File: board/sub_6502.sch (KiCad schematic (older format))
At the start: 17 parts, among them Q1201 Q_NPN_BEC, U1201 74HCT245, U1202 6502, U1203 74HCT245, U1204 74HCT245, U1205 74HCT245

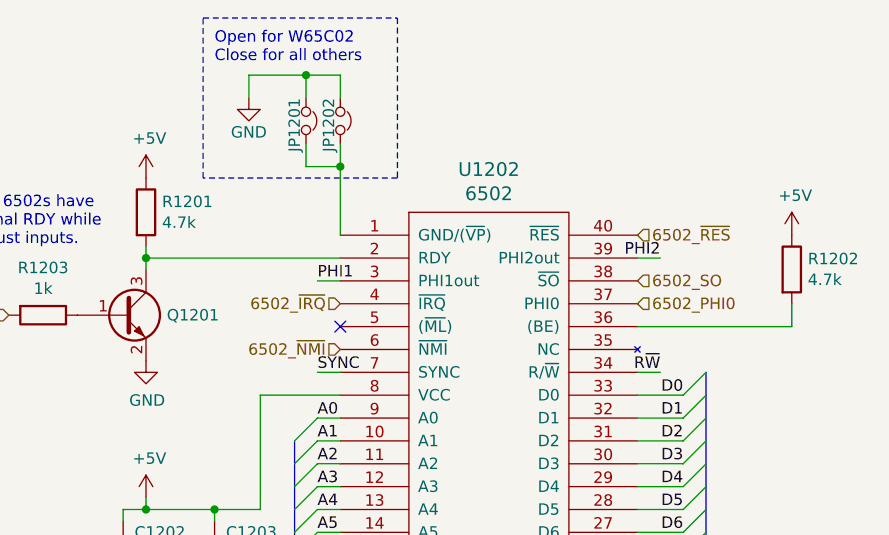
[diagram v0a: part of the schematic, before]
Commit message: Started picking footprints. Merged many components.
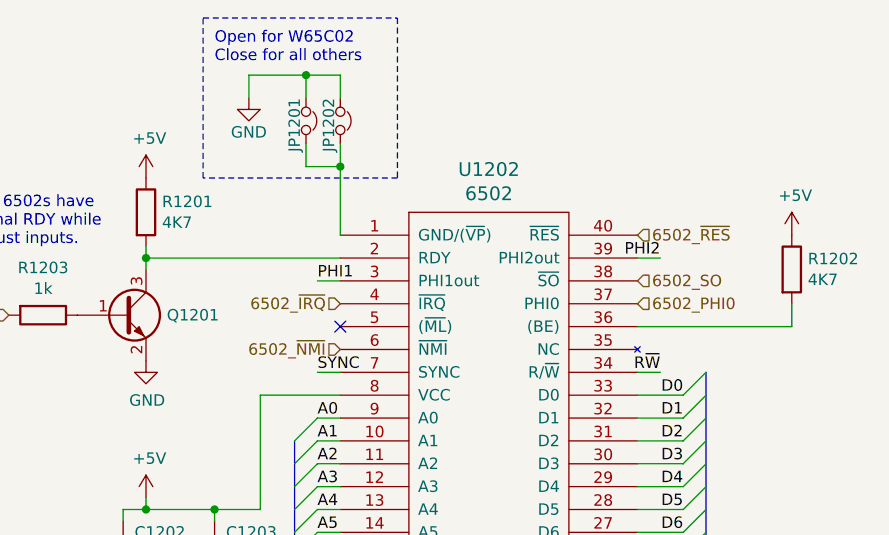
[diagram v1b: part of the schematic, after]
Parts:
- R1201, R1202: value 4.7k -> 4K7
- U1201, U1203, U1204, U1205: footprint (none) -> Package_SO:SSOP-20_4.4x6.5mm_P0.65mm
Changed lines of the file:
@@
 $Descr A4 11693 8268
 encoding utf-8
-Sheet 12 14
+Sheet 12 15
 Title ""
 Date ""
@@
 F 0 "U1202" H 9200 3687 60  0000 C CNN
 F 1 "6502" H 9200 3581 60  0000 C CNN
-F 2 "" H 8700 2700 60  0000 C CNN
+F 2 "" H 8700 2700 60  0001 C CNN
 F 3 "" H 8700 2700 60  0000 C CNN
 	1    9200 2500
@@
 F 0 "U1205" H 9150 5650 50  0000 C CNN
 F 1 "74HCT245" H 9600 5650 50  0000 C CNN
-F 2 "" H 9350 5000 50  0001 C CNN
+F 2 "Package_SO:SSOP-20_4.4x6.5mm_P0.65mm" H 9350 5000 50  0001 C CNN
 F 3 "http://www.ti.com/lit/gpn/sn74HC245" H 9350 5000 50  0001 C CNN
 	1    9350 5000
@@
 F 0 "U1203" H 4900 5650 50  0000 C CNN
 F 1 "74HCT245" H 5350 5650 50  0000 C CNN
-F 2 "" H 5100 5000 50  0001 C CNN
+F 2 "Package_SO:SSOP-20_4.4x6.5mm_P0.65mm" H 5100 5000 50  0001 C CNN
 F 3 "http://www.ti.com/lit/gpn/sn74HC245" H 5100 5000 50  0001 C CNN
 	1    5100 5000
@@
 F 0 "U1204" H 6700 5650 50  0000 C CNN
 F 1 "74HCT245" H 7150 5650 50  0000 C CNN
-F 2 "" H 6900 5000 50  0001 C CNN
+F 2 "Package_SO:SSOP-20_4.4x6.5mm_P0.65mm" H 6900 5000 50  0001 C CNN
 F 3 "http://www.ti.com/lit/gpn/sn74HC245" H 6900 5000 50  0001 C CNN
 	1    6900 5000
@@
 F 0 "U1201" H 5100 3000 50  0000 C CNN
 F 1 "74HCT245" H 5550 3000 50  0000 C CNN
-F 2 "" H 5300 2350 50  0001 C CNN
+F 2 "Package_SO:SSOP-20_4.4x6.5mm_P0.65mm" H 5300 2350 50  0001 C CNN
 F 3 "http://www.ti.com/lit/gpn/sn74HC245" H 5300 2350 50  0001 C CNN
 	1    5300 2350
@@
 P 7700 1500
 F 0 "R1201" H 7770 1546 50  0000 L CNN
-F 1 "4.7k" H 7770 1455 50  0000 L CNN
+F 1 "4K7" H 7770 1455 50  0000 L CNN
 F 2 "" V 7630 1500 50  0001 C CNN
 F 3 "~" H 7700 1500 50  0001 C CNN
@@
 P 10525 1750
 F 0 "R1202" H 10595 1796 50  0000 L CNN
-F 1 "4.7k" H 10595 1705 50  0000 L CNN
+F 1 "4K7" H 10595 1705 50  0000 L CNN
 F 2 "" V 10455 1750 50  0001 C CNN
 F 3 "~" H 10525 1750 50  0001 C CNN

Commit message: More footprints done. Went with simpler test-pads.
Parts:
- JP1201, JP1202: footprint (none) -> Connector_PinHeader_2.54mm:PinHeader_1x02_P2.54mm_Vertical
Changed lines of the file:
@@
 $Descr A4 11693 8268
 encoding utf-8
-Sheet 12 15
+Sheet 12 14
 Title ""
 Date ""
@@
 F 0 "JP1201" H 8300 1050 50  0000 L CNN
 F 1 "Jumper_NC_Small" H 8400 1221 50  0001 C CNN
-F 2 "" H 8400 1100 50  0001 C CNN
+F 2 "Connector_PinHeader_2.54mm:PinHeader_1x02_P2.54mm_Vertical" H 8400 1100 50  0001 C CNN
 F 3 "~" H 8400 1100 50  0001 C CNN
 	1    8400 1100
@@
 F 0 "JP1202" H 8450 1050 50  0000 L CNN
 F 1 "WireJumper" H 8550 1200 50  0001 C CNN
-F 2 "" H 8550 1100 50  0001 C CNN
+F 2 "Connector_PinHeader_2.54mm:PinHeader_1x02_P2.54mm_Vertical" H 8550 1100 50  0001 C CNN
 F 3 "~" H 8550 1100 50  0001 C CNN
 	1    8550 1100

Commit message: Most footprints associated
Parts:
- C1201, C1202, C1204, C1205, C1206: footprint (none) -> Capacitor_SMD:C_0603_1608Metric
- C1203: footprint (none) -> Capacitor_SMD:C_1206_3216Metric
- Q1201: footprint (none) -> Package_TO_SOT_SMD:SOT-23
- R1201, R1202, R1203: footprint (none) -> Resistor_SMD:R_0603_1608Metric
- U1202: footprint (none) -> Package_DIP:DIP-40_W15.24mm
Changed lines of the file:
@@
 F 0 "U1202" H 9200 3687 60  0000 C CNN
 F 1 "6502" H 9200 3581 60  0000 C CNN
-F 2 "" H 8700 2700 60  0001 C CNN
+F 2 "Package_DIP:DIP-40_W15.24mm" H 8700 2700 60  0001 C CNN
 F 3 "" H 8700 2700 60  0000 C CNN
 	1    9200 2500
@@
 F 0 "R1203" V 7043 1950 50  0000 C CNN
 F 1 "1k" V 7134 1950 50  0000 C CNN
-F 2 "" V 7180 1950 50  0001 C CNN
+F 2 "Resistor_SMD:R_0603_1608Metric" V 7180 1950 50  0001 C CNN
 F 3 "~" H 7250 1950 50  0001 C CNN
 	1    7250 1950
@@
 F 0 "Q1201" H 7791 1950 50  0000 L CNN
 F 1 "Q_NPN_BEC" H 7791 1905 50  0001 L CNN
-F 2 "" H 7800 2050 50  0001 C CNN
+F 2 "Package_TO_SOT_SMD:SOT-23" H 7800 2050 50  0001 C CNN
 F 3 "~" H 7600 1950 50  0001 C CNN
 	1    7600 1950
@@
 F 0 "R1201" H 7770 1546 50  0000 L CNN
 F 1 "4K7" H 7770 1455 50  0000 L CNN
-F 2 "" V 7630 1500 50  0001 C CNN
+F 2 "Resistor_SMD:R_0603_1608Metric" V 7630 1500 50  0001 C CNN
 F 3 "~" H 7700 1500 50  0001 C CNN
 	1    7700 1500
@@
 F 0 "R1202" H 10595 1796 50  0000 L CNN
 F 1 "4K7" H 10595 1705 50  0000 L CNN
-F 2 "" V 10455 1750 50  0001 C CNN
+F 2 "Resistor_SMD:R_0603_1608Metric" V 10455 1750 50  0001 C CNN
 F 3 "~" H 10525 1750 50  0001 C CNN
 	1    10525 1750
@@
 F 0 "C1203" H 8050 3100 50  0000 L CNN
 F 1 "10u" H 8050 2900 50  0000 L CNN
-F 2 "" H 8038 2850 50  0001 C CNN
+F 2 "Capacitor_SMD:C_1206_3216Metric" H 8038 2850 50  0001 C CNN
 F 3 "~" H 8000 3000 50  0001 C CNN
 	1    8000 3000
@@
 F 0 "C1202" H 7650 3100 50  0000 L CNN
 F 1 "0.1u" H 7650 2900 50  0000 L CNN
-F 2 "" H 7638 2850 50  0001 C CNN
+F 2 "Capacitor_SMD:C_0603_1608Metric" H 7638 2850 50  0001 C CNN
 F 3 "~" H 7600 3000 50  0001 C CNN
 	1    7600 3000
@@
 F 0 "C1201" H 6315 2396 50  0000 L CNN
 F 1 "1u" H 6315 2305 50  0000 L CNN
-F 2 "" H 6238 2200 50  0001 C CNN
+F 2 "Capacitor_SMD:C_0603_1608Metric" H 6238 2200 50  0001 C CNN
 F 3 "~" H 6200 2350 50  0001 C CNN
 	1    6200 2350
@@
 F 0 "C1204" H 4000 5100 50  0000 L CNN
 F 1 "1u" H 4000 4900 50  0000 L CNN
-F 2 "" H 3988 4850 50  0001 C CNN
+F 2 "Capacitor_SMD:C_0603_1608Metric" H 3988 4850 50  0001 C CNN
 F 3 "~" H 3950 5000 50  0001 C CNN
 	1    3950 5000
@@
 F 0 "C1205" H 8015 5046 50  0000 L CNN
 F 1 "1u" H 8015 4955 50  0000 L CNN
-F 2 "" H 7938 4850 50  0001 C CNN
+F 2 "Capacitor_SMD:C_0603_1608Metric" H 7938 4850 50  0001 C CNN
 F 3 "~" H 7900 5000 50  0001 C CNN
 	1    7900 5000
@@
 F 0 "C1206" H 10465 5046 50  0000 L CNN
 F 1 "1u" H 10465 4955 50  0000 L CNN
-F 2 "" H 10388 4850 50  0001 C CNN
+F 2 "Capacitor_SMD:C_0603_1608Metric" H 10388 4850 50  0001 C CNN
 F 3 "~" H 10350 5000 50  0001 C CNN
 	1    10350 5000

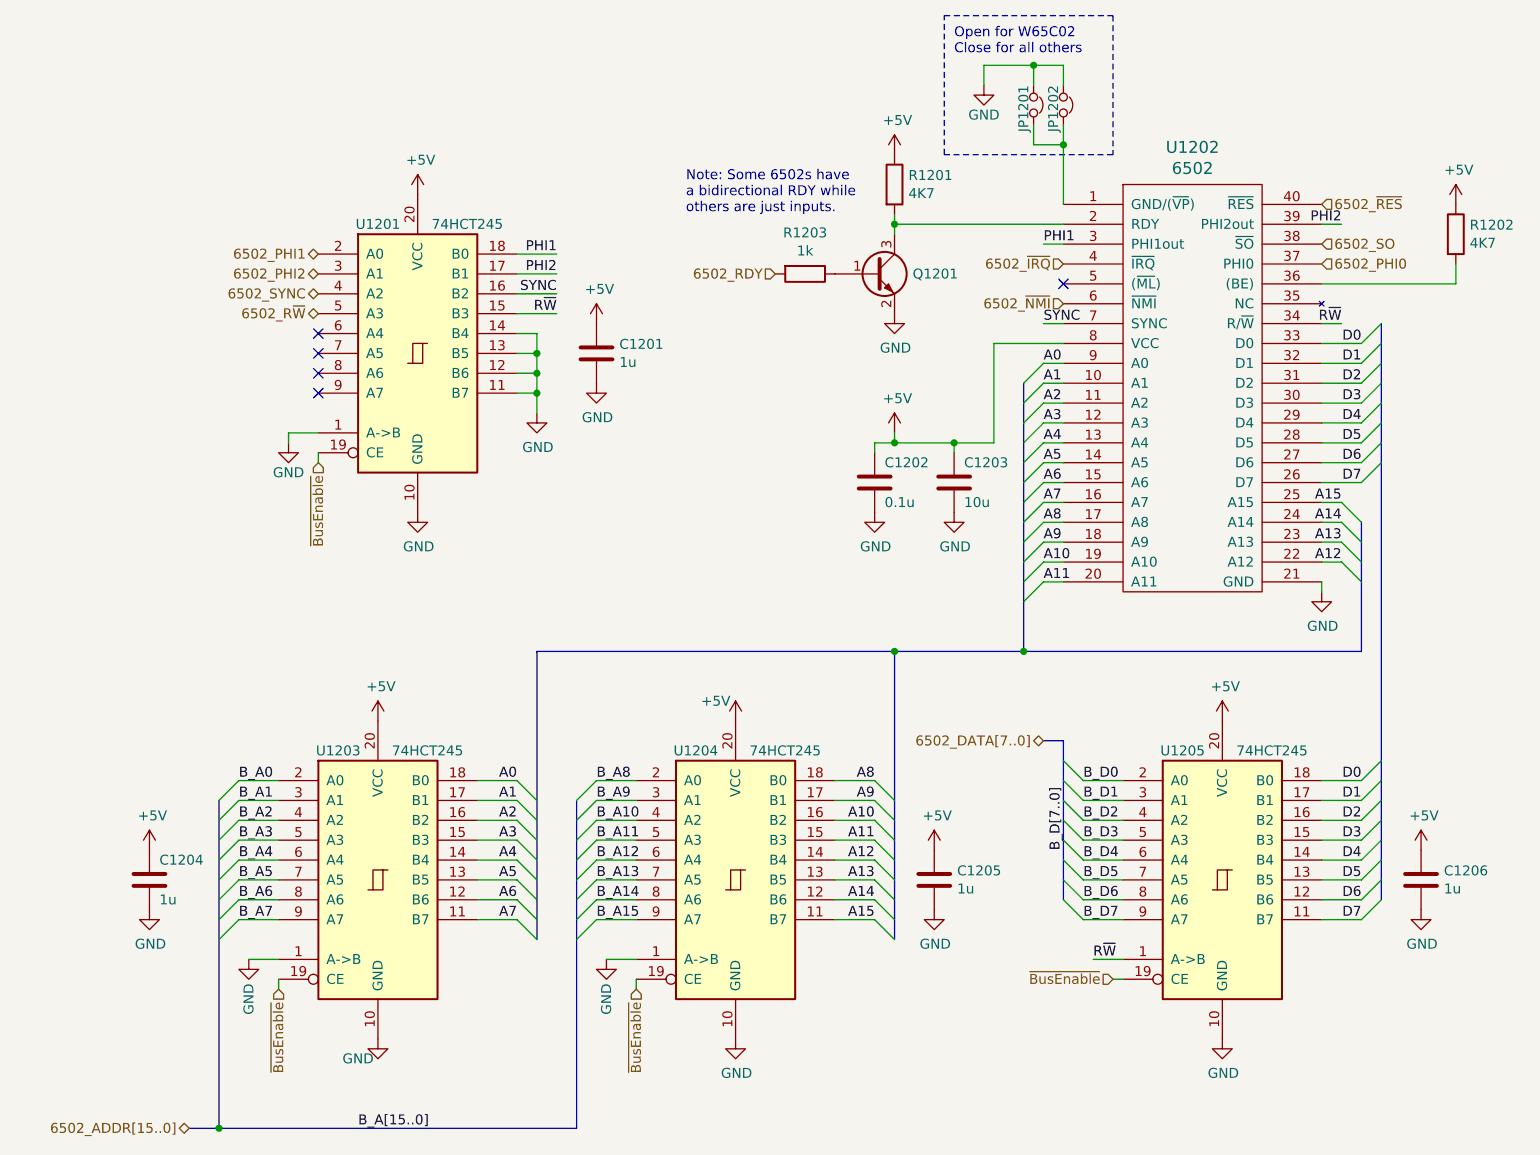
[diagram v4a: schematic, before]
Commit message: Power supply routed
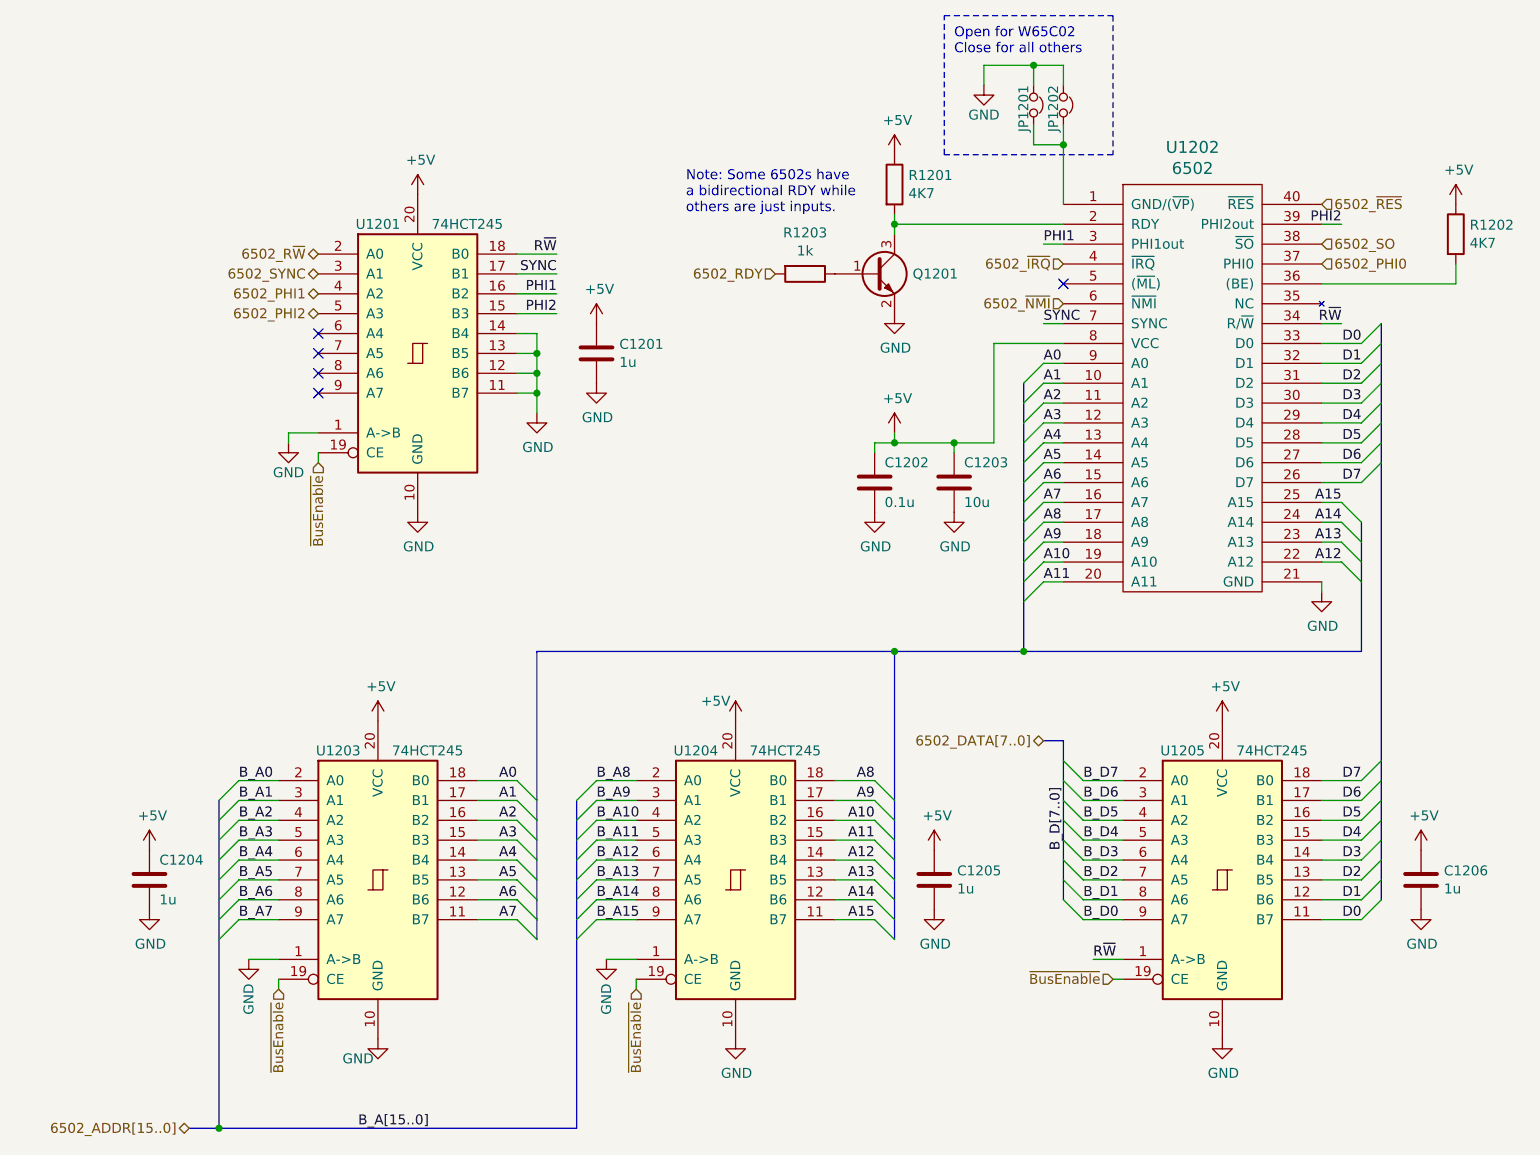
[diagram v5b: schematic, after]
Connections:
- net 6502_PHI1: now also U1201.4 (A2); no longer U1201.2 (A0)
- net 6502_PHI2: now also U1201.5 (A3); no longer U1201.3 (A1)
- net 6502_R~W: now also U1201.2 (A0); no longer U1201.5 (A3)
- net 6502_SYNC: now also U1201.3 (A1); no longer U1201.4 (A2)
- net B_D0: now also U1205.9 (A7); no longer U1205.2 (A0)
- net B_D1: now also U1205.8 (A6); no longer U1205.3 (A1)
- net B_D2: now also U1205.7 (A5); no longer U1205.4 (A2)
- net B_D3: now also U1205.6 (A4); no longer U1205.5 (A3)
- net B_D4: now also U1205.5 (A3); no longer U1205.6 (A4)
- net B_D5: now also U1205.4 (A2); no longer U1205.7 (A5)
- net B_D6: now also U1205.3 (A1); no longer U1205.8 (A6)
- net B_D7: now also U1205.2 (A0); no longer U1205.9 (A7)
- net D0: now also U1205.11 (B7); no longer U1205.18 (B0)
- net D1: now also U1205.12 (B6); no longer U1205.17 (B1)
- net D2: now also U1205.13 (B5); no longer U1205.16 (B2)
- net D3: now also U1205.14 (B4); no longer U1205.15 (B3)
- net D4: now also U1205.15 (B3); no longer U1205.14 (B4)
- net D5: now also U1205.16 (B2); no longer U1205.13 (B5)
- net D6: now also U1205.17 (B1); no longer U1205.12 (B6)
- net D7: now also U1205.18 (B0); no longer U1205.11 (B7)
- net PHI1: now also U1201.16 (B2); no longer U1201.18 (B0)
- net PHI2: now also U1201.15 (B3); no longer U1201.17 (B1)
- net R~W: now also U1201.18 (B0); no longer U1201.15 (B3)
- net SYNC: now also U1201.17 (B1); no longer U1201.16 (B2)
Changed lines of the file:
@@
 Text HLabel 4150 6250 0    50   3State ~ 0
 6502_ADDR[15..0]
-Text HLabel 4800 2150 0    50   3State ~ 0
+Text HLabel 4800 1850 0    50   3State ~ 0
 6502_R~W
 Text HLabel 7100 1950 0    50   Input ~ 0
 6502_RDY
-Text HLabel 4800 1850 0    50   3State ~ 0
+Text HLabel 4800 2050 0    50   3State ~ 0
 6502_PHI1
 Text HLabel 9850 1900 2    50   Input ~ 0
 6502_PHI0
-Text HLabel 4800 1950 0    50   3State ~ 0
+Text HLabel 4800 2150 0    50   3State ~ 0
 6502_PHI2
 Text HLabel 8550 1900 0    50   Input ~ 0
@@
 Entry Wire Line
 	10050 5200 10150 5100
+Text Label 10050 5200 2    50   ~ 0
+D0
+Text Label 10050 5100 2    50   ~ 0
+D1
+Text Label 10050 5000 2    50   ~ 0
+D2
+Text Label 10050 4900 2    50   ~ 0
+D3
+Text Label 10050 4800 2    50   ~ 0
+D4
+Text Label 10050 4700 2    50   ~ 0
+D5
+Text Label 10050 4600 2    50   ~ 0
+D6
 Text Label 10050 4500 2    50   ~ 0
-D0
-Text Label 10050 4600 2    50   ~ 0
-D1
-Text Label 10050 4700 2    50   ~ 0
-D2
-Text Label 10050 4800 2    50   ~ 0
-D3
-Text Label 10050 4900 2    50   ~ 0
-D4
-Text Label 10050 5000 2    50   ~ 0
-D5
-Text Label 10050 5100 2    50   ~ 0
-D6
-Text Label 10050 5200 2    50   ~ 0
 D7
 Entry Wire Line
@@
 	8650 5200 8550 5100
 Wire Wire Line
-	8650 5200 8850 5200
-Wire Wire Line
-	8850 5100 8650 5100
-Wire Wire Line
-	8650 5000 8850 5000
-Wire Wire Line
-	8850 4900 8650 4900
-Wire Wire Line
-	8650 4800 8850 4800
-Wire Wire Line
-	8850 4700 8650 4700
-Wire Wire Line
-	8650 4600 8850 4600
-Wire Wire Line
-	8850 4500 8650 4500
+	8650 4500 8850 4500
+Wire Wire Line
+	8850 4600 8650 4600
+Wire Wire Line
+	8650 4700 8850 4700
+Wire Wire Line
+	8850 4800 8650 4800
+Wire Wire Line
+	8650 4900 8850 4900
+Wire Wire Line
+	8850 5000 8650 5000
+Wire Wire Line
+	8650 5100 8850 5100
+Wire Wire Line
+	8850 5200 8650 5200
+Text Label 8650 5200 0    50   ~ 0
+B_D0
+Text Label 8650 5100 0    50   ~ 0
+B_D1
+Text Label 8650 5000 0    50   ~ 0
+B_D2
+Text Label 8650 4900 0    50   ~ 0
+B_D3
+Text Label 8650 4800 0    50   ~ 0
+B_D4
+Text Label 8650 4700 0    50   ~ 0
+B_D5
+Text Label 8650 4600 0    50   ~ 0
+B_D6
 Text Label 8650 4500 0    50   ~ 0
-B_D0
-Text Label 8650 4600 0    50   ~ 0
-B_D1
-Text Label 8650 4700 0    50   ~ 0
-B_D2
-Text Label 8650 4800 0    50   ~ 0
-B_D3
-Text Label 8650 4900 0    50   ~ 0
-B_D4
-Text Label 8650 5000 0    50   ~ 0
-B_D5
-Text Label 8650 5100 0    50   ~ 0
-B_D6
-Text Label 8650 5200 0    50   ~ 0
 B_D7
 Wire Bus Line
@@
 	1    0    0    -1
 $EndComp
-Text HLabel 4800 2050 0    50   3State ~ 0
+Text HLabel 4800 1950 0    50   3State ~ 0
 6502_SYNC
 Text HLabel 4800 2900 3    50   Input ~ 0
@@
 Text Label 8450 2200 0    50   ~ 0
 SYNC
-Text Label 6000 1850 2    50   ~ 0
+Text Label 6000 2050 2    50   ~ 0
 PHI1
 Text Label 9950 1700 2    50   ~ 0
 PHI2
+Text Label 6000 2150 2    50   ~ 0
+PHI2
 Text Label 6000 1950 2    50   ~ 0
-PHI2
-Text Label 6000 2050 2    50   ~ 0
 SYNC
-Text Label 6000 2150 2    50   ~ 0
+Text Label 6000 1850 2    50   ~ 0
 R~W
 Wire Wire Line
+	6000 2050 5800 2050
+Wire Wire Line
+	5800 2150 6000 2150
+Wire Wire Line
+	6000 1950 5800 1950
+Wire Wire Line
 	6000 1850 5800 1850
-Wire Wire Line
-	5800 1950 6000 1950
-Wire Wire Line
-	6000 2050 5800 2050
-Wire Wire Line
-	6000 2150 5800 2150
 $Comp
 L Device:R R1203
